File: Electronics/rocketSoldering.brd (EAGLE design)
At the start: 97.3 x 97.3 mm, 6 parts

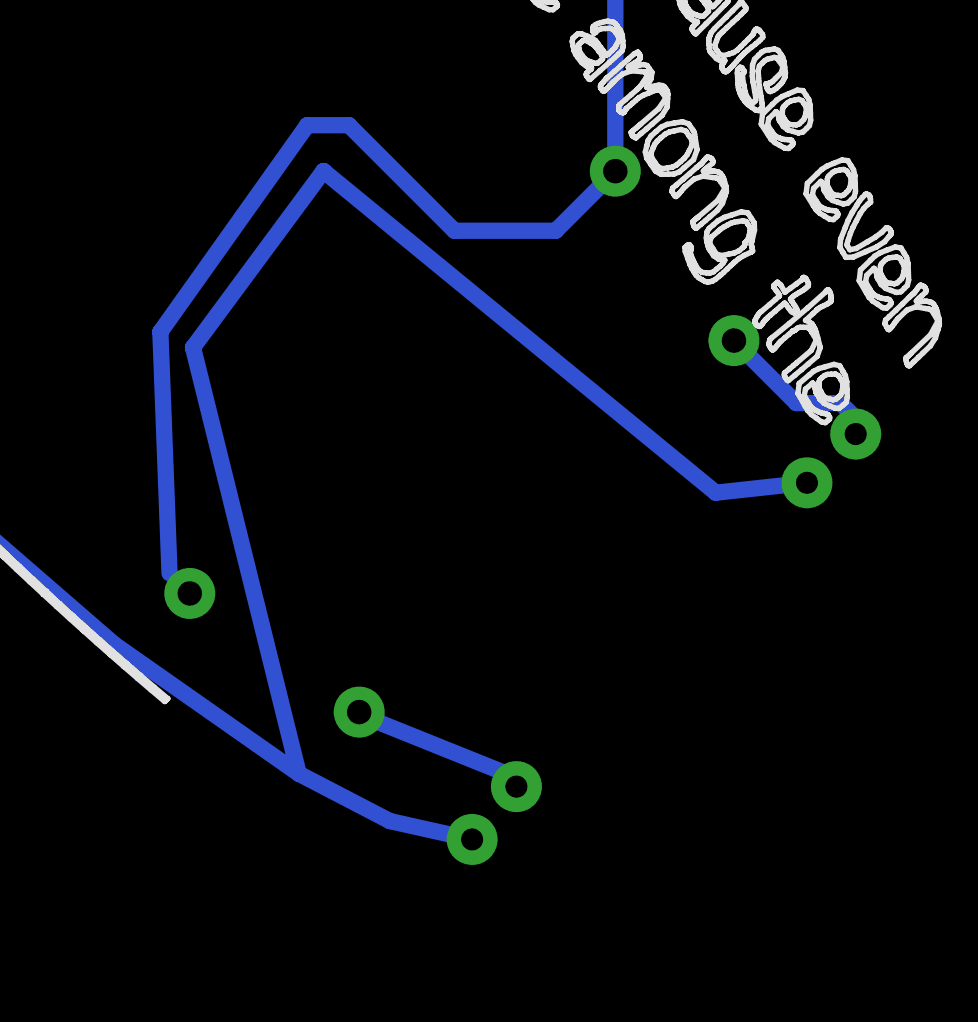
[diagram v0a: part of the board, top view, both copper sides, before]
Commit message: Changed resistor to SMD
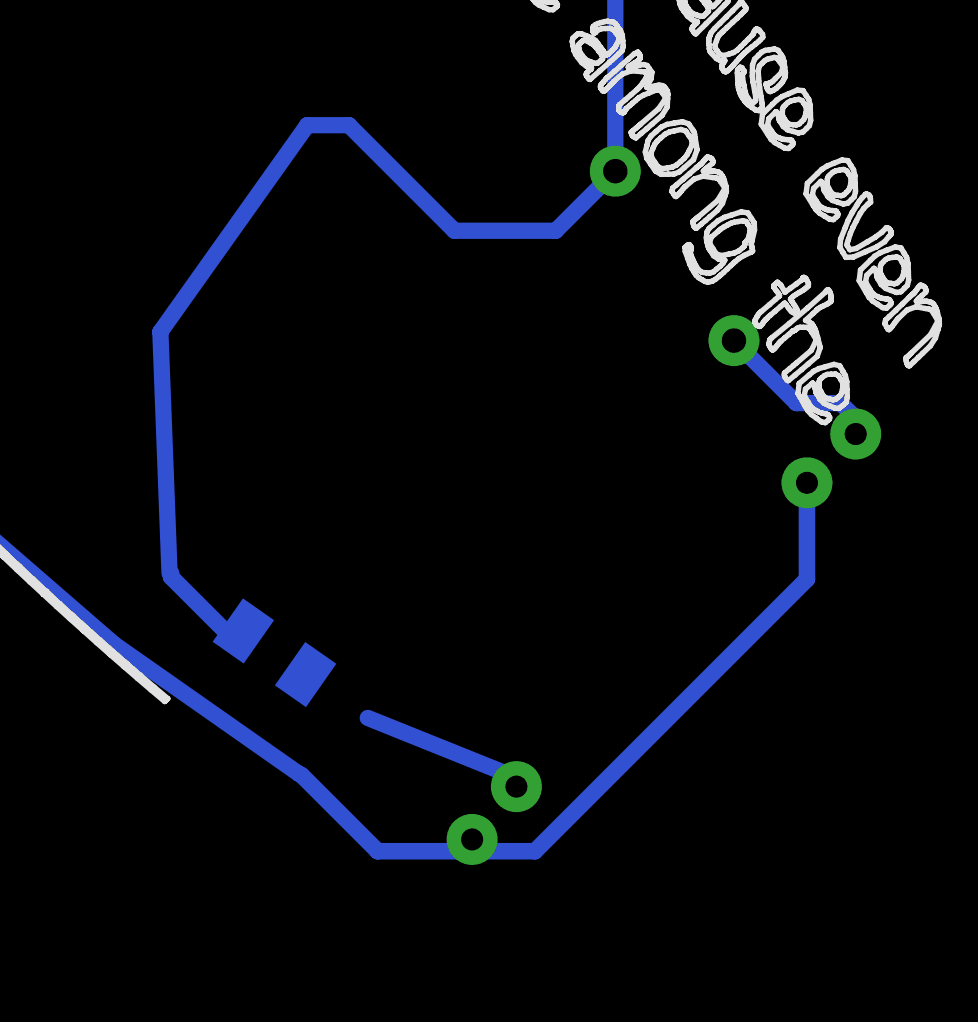
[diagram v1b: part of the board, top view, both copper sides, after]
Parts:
- R2: device SparkFun-Passives:AXIAL-0.3 -> Common-Parts-Library-Eagle:CRCW12060000Z0EA_RESC3216X65
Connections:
- net N$1: now also R2.2; no longer R2.P$2
- net N$2: now also R2.1; no longer R2.P$1
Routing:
- net GND: track 114.0 -> 88.4 mm
- net N$2: track 52.1 -> 55.3 mm
- net N$1: track 7.45 -> 6.47 mm
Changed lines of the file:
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@@
 <attribute name="VALUE" x="64.79101875" y="41.66374375" size="1.27" layer="28" ratio="10" rot="MR315"/>
 </element>
-<element name="R2" library="SparkFun-Passives" package="AXIAL-0.3" value="10k" x="45.263428125" y="38.04196875" smashed="yes" rot="MR215"/>
+<element name="R2" library="Common-Parts-Library-Eagle" package="CRCW12060000Z0EA_RESC3216X65" value="10k" x="45.263428125" y="38.04196875" smashed="yes" rot="MR215">
+<attribute name="MANUFACTURER" value="VISHAY" x="45.263428125" y="38.04196875" size="1.778" layer="28" rot="MR215" display="off"/>
+</element>
 <element name="S2" library="TinkerElectric" package="OS102011MA1QN1" value="OS102011MA1QN1" x="55.087840625" y="74.1947875" smashed="yes" rot="MR225">
 <attribute name="RS_PRICE-STOCK" value="http://uk.rs-online.com/web/p/products/7874855" x="55.087840625" y="74.1947875" size="1.778" layer="28" rot="MR225" display="off"/>
@@
 <wire x1="27.259940625" y1="48.84778125" x2="39.3660625" y2="38.350165625" width="0.6" layer="16"/>
 <wire x1="39.3660625" y1="38.350165625" x2="46.15565" y2="33.588353125" width="0.6" layer="16"/>
-<wire x1="46.15565" y1="33.588353125" x2="49.51461875" y2="31.841909375" width="0.6" layer="16"/>
-<wire x1="49.51461875" y1="31.841909375" x2="52.54391875" y2="31.16464375" width="0.6" layer="16"/>
-<wire x1="64.880821875" y1="44.3039375" x2="61.52219375" y2="43.93760625" width="0.6" layer="16"/>
-<wire x1="61.52219375" y1="43.93760625" x2="47.069959375" y2="55.789753125" width="0.6" layer="16"/>
-<wire x1="47.069959375" y1="55.789753125" x2="42.261375" y2="49.288" width="0.6" layer="16"/>
-<wire x1="42.261375" y1="49.288" x2="46.15565" y2="33.588353125" width="0.6" layer="16"/>
+<wire x1="46.15565" y1="33.588353125" x2="46.26703125" y2="33.53044375" width="0.6" layer="16"/>
 <polygon width="0" layer="1">
 <vertex x="-0.169315625" y="96.425690625"/>
@@
 <vertex x="0.084659375" y="96.9336375"/>
 </polygon>
+<wire x1="64.880821875" y1="44.3039375" x2="64.880821875" y2="40.7532375" width="0.6096" layer="16"/>
+<wire x1="64.880821875" y1="40.7532375" x2="54.8585125" y2="30.730928125" width="0.6096" layer="16"/>
+<wire x1="54.8585125" y1="30.730928125" x2="49.066546875" y2="30.730928125" width="0.6096" layer="16"/>
+<wire x1="49.066546875" y1="30.730928125" x2="46.26703125" y2="33.53044375" width="0.6096" layer="16"/>
 </signal>
 <signal name="N$1">
-<contactref element="R2" pad="P$2"/>
-<contactref element="R2" pad="P$2"/>
+<contactref element="R2" pad="2"/>
+<contactref element="R2" pad="2"/>
 <contactref element="D1" pad="A"/>
-<wire x1="48.3844" y1="35.3241625" x2="48.3844" y2="35.856640625" width="0.254" layer="16"/>
-<wire x1="48.3844" y1="35.3241625" x2="48.701340625" y2="35.641103125" width="0.6" layer="16"/>
 <wire x1="48.701340625" y1="35.641103125" x2="53.75795625" y2="33.60930625" width="0.6" layer="16"/>
 <wire x1="53.75795625" y1="33.60930625" x2="54.176596875" y2="33.698615625" width="0.6" layer="16"/>
 <wire x1="54.176596875" y1="33.698615625" x2="54.176596875" y2="33.110396875" width="0.6" layer="16"/>
+<wire x1="46.41024375" y1="37.238959375" x2="48.701340625" y2="35.641103125" width="0" layer="19" extent="16-16"/>
 </signal>
 <signal name="N$2">
-<contactref element="R2" pad="P$1"/>
-<contactref element="R2" pad="P$1"/>
+<contactref element="R2" pad="1"/>
+<contactref element="R2" pad="1"/>
 <contactref element="R4" pad="P$1"/>
 <contactref element="S2" pad="3"/>
@@
 <wire x1="57.820296875" y1="67.050546875" x2="57.820296875" y2="55.78434375" width="0.6" layer="16"/>
 <wire x1="57.699509375" y1="55.78434375" x2="57.820296875" y2="55.78434375" width="0.254" layer="16"/>
-<wire x1="42.142459375" y1="40.22729375" x2="41.82115" y2="40.548603125" width="0.6" layer="16"/>
 <wire x1="57.820296875" y1="55.78434375" x2="55.62459375" y2="53.588640625" width="0.6" layer="16"/>
 <wire x1="55.62459375" y1="53.588640625" x2="51.895478125" y2="53.588640625" width="0.6" layer="16"/>
 <wire x1="51.895478125" y1="53.588640625" x2="48.006609375" y2="57.477509375" width="0.6" layer="16"/>
-<wire x1="41.82115" y1="40.548603125" x2="41.397859375" y2="40.97189375" width="0.254" layer="16"/>
 <wire x1="41.397859375" y1="40.97189375" x2="41.059225" y2="49.86368125" width="0.6" layer="16"/>
 <wire x1="41.059225" y1="49.86368125" x2="46.47194375" y2="57.477509375" width="0.6" layer="16"/>
 <wire x1="46.47194375" y1="57.477509375" x2="48.006609375" y2="57.477509375" width="0.6" layer="16"/>
+<wire x1="41.397859375" y1="40.97189375" x2="41.456575" y2="40.97189375" width="0.254" layer="16"/>
+<wire x1="41.456575" y1="40.97189375" x2="41.456575" y2="40.831196875" width="0.6096" layer="16"/>
+<wire x1="41.456575" y1="40.831196875" x2="43.93760625" y2="38.350165625" width="0.6096" layer="16"/>
+<wire x1="43.93760625" y1="38.350165625" x2="43.93760625" y2="38.665965625" width="0.6096" layer="16"/>
+<wire x1="43.93760625" y1="38.665965625" x2="44.116615625" y2="38.844975" width="0.6096" layer="16"/>
 </signal>
 <signal name="N$5">
